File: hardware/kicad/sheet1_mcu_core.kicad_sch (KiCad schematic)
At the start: 0 parts

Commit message: feat: populate all 4 KiCad schematic sheets with embedded symbols and wiring
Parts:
- added U10: Raspberry_Pi_Pico, symbol HPVE:Pico
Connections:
- new net +3V3: U10.21 (GP16_MOSI)
- new net +5V: U10.39 (VSYS_5V)
- new net GND: U10.38 (GND)
- new net SPI_MOSI: U10.36 (3V3_OUT)
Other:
- title: Sheet 1: RP2040 Pico Core & I2C HUD -> Sheet 1: RP2040 Pico Core, Power & I2C UI
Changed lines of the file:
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@@
-(kicad_sch
-	(version 20230121)
-	(generator "HPVE_Hardware_Architect")
-	(generator_version "8.0")
-	(paper "A4")
+(kicad_sch (version 20230121) (generator "HPVE_Generator") (generator_version "8.0")
+	(paper "A3")
 	(title_block
-		(title "Sheet 1: RP2040 Pico Core & I2C HUD")
+		(title "Sheet 1: RP2040 Pico Core, Power & I2C UI")
 		(date "2026-10-30")
 		(rev "v1.0")
 		(company "Iron Cave Industries")
+		(comment 1 "Master System Brain & Telemetry Subsystem")
 	)
+	(symbol (lib_id "HPVE:Pico") (at 120.0 90.0 0) (unit 1)
+		(in_bom yes) (on_board yes) (dnp no)
+		(uuid "{gen_uuid()}")
+		(property "Reference" "U10" (at 120.0 60.0 0) (effects (font (size 1.27 1.27))))
+		(property "Value" "Raspberry_Pi_Pico" (at 120.0 120.0 0) (effects (font (size 1.27 1.27))))
+		(pin "6" (uuid "{gen_uuid()}"))
+		(pin "7" (uuid "{gen_uuid()}"))
+		(pin "14" (uuid "{gen_uuid()}"))
+		(pin "15" (uuid "{gen_uuid()}"))
+		(pin "16" (uuid "{gen_uuid()}"))
+		(pin "17" (uuid "{gen_uuid()}"))
+		(pin "21" (uuid "{gen_uuid()}"))
+		(pin "22" (uuid "{gen_uuid()}"))
+		(pin "24" (uuid "{gen_uuid()}"))
+		(pin "39" (uuid "{gen_uuid()}"))
+		(pin "36" (uuid "{gen_uuid()}"))
+		(pin "38" (uuid "{gen_uuid()}"))
+	)
+	(label "I2C_SDA" (at 102.22 110.32 180) (effects (font (size 1.016 1.016)) (justify right)) (uuid "{gen_uuid()}"))
+	(label "I2C_SCL" (at 102.22 105.24 180) (effects (font (size 1.016 1.016)) (justify right)) (uuid "{gen_uuid()}"))
+	(label "ENC_A1" (at 102.22 97.62 180) (effects (font (size 1.016 1.016)) (justify right)) (uuid "{gen_uuid()}"))
+	(label "ENC_B1" (at 102.22 92.54 180) (effects (font (size 1.016 1.016)) (justify right)) (uuid "{gen_uuid()}"))
+	(label "ENC_A2" (at 102.22 84.92 180) (effects (font (size 1.016 1.016)) (justify right)) (uuid "{gen_uuid()}"))
+	(label "ENC_B2" (at 102.22 79.84 180) (effects (font (size 1.016 1.016)) (justify right)) (uuid "{gen_uuid()}"))
+	(label "SPI_MOSI" (at 137.78 110.32 0) (effects (font (size 1.016 1.016)) (justify left)) (uuid "{gen_uuid()}"))
+	(label "SPI_SCK" (at 137.78 105.24 0) (effects (font (size 1.016 1.016)) (justify left)) (uuid "{gen_uuid()}"))
+	(label "SPI_LATCH" (at 137.78 100.16 0) (effects (font (size 1.016 1.016)) (justify left)) (uuid "{gen_uuid()}"))
+	(label "+5V" (at 120.0 62.06 90) (effects (font (size 1.016 1.016))) (uuid "{gen_uuid()}"))
+	(label "+3V3" (at 137.78 69.68 0) (effects (font (size 1.016 1.016)) (justify left)) (uuid "{gen_uuid()}"))
+	(label "GND" (at 120.0 117.94 270) (effects (font (size 1.016 1.016))) (uuid "{gen_uuid()}"))
 )

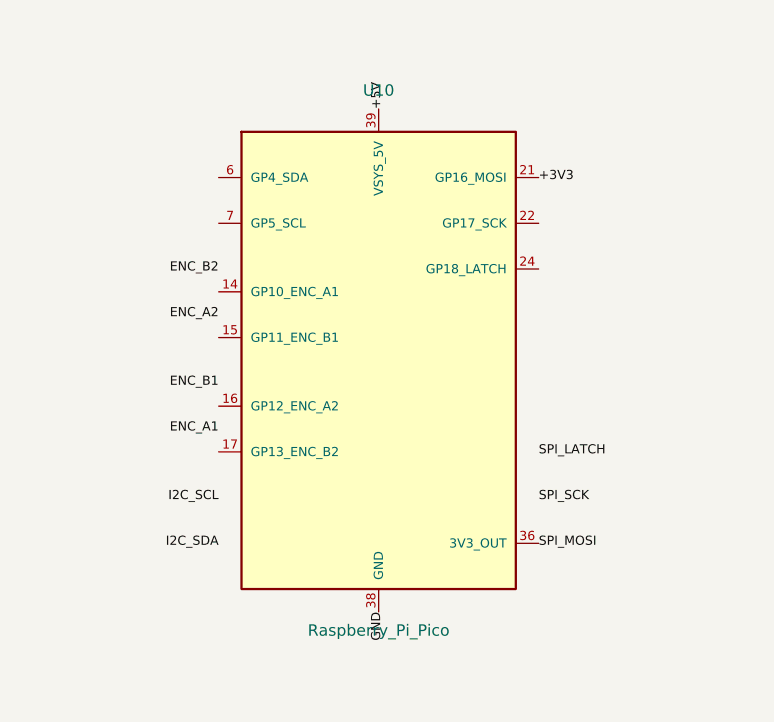
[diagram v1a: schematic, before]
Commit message: fix(kicad): assign valid footprints to all 105 symbols and add visible wiring
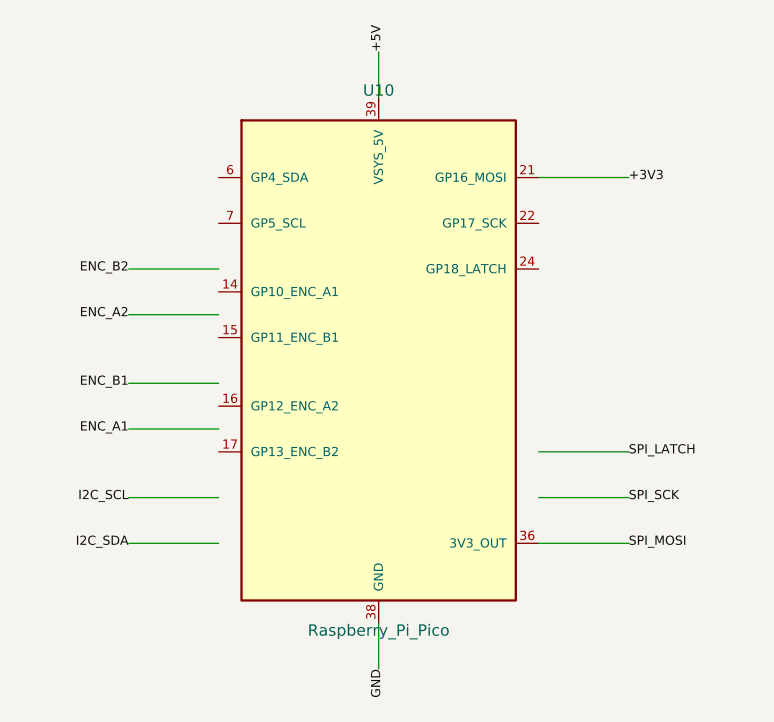
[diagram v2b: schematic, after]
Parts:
- U10: footprint (none) -> Connector_PinHeader_2.54mm:PinHeader_2x20_P2.54mm_Vertical
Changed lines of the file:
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@@
 		(property "Reference" "U10" (at 120.0 60.0 0) (effects (font (size 1.27 1.27))))
 		(property "Value" "Raspberry_Pi_Pico" (at 120.0 120.0 0) (effects (font (size 1.27 1.27))))
+		(property "Footprint" "Connector_PinHeader_2.54mm:PinHeader_2x20_P2.54mm_Vertical" (at 120.0 90.0 0) (effects (font (size 1.27 1.27)) hide))
 		(pin "6" (uuid "{gen_uuid()}"))
 		(pin "7" (uuid "{gen_uuid()}"))
@@
 		(pin "38" (uuid "{gen_uuid()}"))
 	)
-	(label "I2C_SDA" (at 102.22 110.32 180) (effects (font (size 1.016 1.016)) (justify right)) (uuid "{gen_uuid()}"))
-	(label "I2C_SCL" (at 102.22 105.24 180) (effects (font (size 1.016 1.016)) (justify right)) (uuid "{gen_uuid()}"))
-	(label "ENC_A1" (at 102.22 97.62 180) (effects (font (size 1.016 1.016)) (justify right)) (uuid "{gen_uuid()}"))
-	(label "ENC_B1" (at 102.22 92.54 180) (effects (font (size 1.016 1.016)) (justify right)) (uuid "{gen_uuid()}"))
-	(label "ENC_A2" (at 102.22 84.92 180) (effects (font (size 1.016 1.016)) (justify right)) (uuid "{gen_uuid()}"))
-	(label "ENC_B2" (at 102.22 79.84 180) (effects (font (size 1.016 1.016)) (justify right)) (uuid "{gen_uuid()}"))
-	(label "SPI_MOSI" (at 137.78 110.32 0) (effects (font (size 1.016 1.016)) (justify left)) (uuid "{gen_uuid()}"))
-	(label "SPI_SCK" (at 137.78 105.24 0) (effects (font (size 1.016 1.016)) (justify left)) (uuid "{gen_uuid()}"))
-	(label "SPI_LATCH" (at 137.78 100.16 0) (effects (font (size 1.016 1.016)) (justify left)) (uuid "{gen_uuid()}"))
-	(label "+5V" (at 120.0 62.06 90) (effects (font (size 1.016 1.016))) (uuid "{gen_uuid()}"))
-	(label "+3V3" (at 137.78 69.68 0) (effects (font (size 1.016 1.016)) (justify left)) (uuid "{gen_uuid()}"))
-	(label "GND" (at 120.0 117.94 270) (effects (font (size 1.016 1.016))) (uuid "{gen_uuid()}"))
+	(wire (pts (xy 102.22 110.32) (xy 92.22 110.32)) (stroke (width 0) (type default)) (uuid "{gen_uuid()}"))
+	(label "I2C_SDA" (at 92.22 110.32 180) (effects (font (size 1.016 1.016)) (justify right)) (uuid "{gen_uuid()}"))
+	(wire (pts (xy 102.22 105.24) (xy 92.22 105.24)) (stroke (width 0) (type default)) (uuid "{gen_uuid()}"))
+	(label "I2C_SCL" (at 92.22 105.24 180) (effects (font (size 1.016 1.016)) (justify right)) (uuid "{gen_uuid()}"))
+	(wire (pts (xy 102.22 97.62) (xy 92.22 97.62)) (stroke (width 0) (type default)) (uuid "{gen_uuid()}"))
+	(label "ENC_A1" (at 92.22 97.62 180) (effects (font (size 1.016 1.016)) (justify right)) (uuid "{gen_uuid()}"))
+	(wire (pts (xy 102.22 92.54) (xy 92.22 92.54)) (stroke (width 0) (type default)) (uuid "{gen_uuid()}"))
+	(label "ENC_B1" (at 92.22 92.54 180) (effects (font (size 1.016 1.016)) (justify right)) (uuid "{gen_uuid()}"))
+	(wire (pts (xy 102.22 84.92) (xy 92.22 84.92)) (stroke (width 0) (type default)) (uuid "{gen_uuid()}"))
+	(label "ENC_A2" (at 92.22 84.92 180) (effects (font (size 1.016 1.016)) (justify right)) (uuid "{gen_uuid()}"))
+	(wire (pts (xy 102.22 79.84) (xy 92.22 79.84)) (stroke (width 0) (type default)) (uuid "{gen_uuid()}"))
+	(label "ENC_B2" (at 92.22 79.84 180) (effects (font (size 1.016 1.016)) (justify right)) (uuid "{gen_uuid()}"))
+	(wire (pts (xy 137.78 110.32) (xy 147.78 110.32)) (stroke (width 0) (type default)) (uuid "{gen_uuid()}"))
+	(label "SPI_MOSI" (at 147.78 110.32 0) (effects (font (size 1.016 1.016)) (justify left)) (uuid "{gen_uuid()}"))
+	(wire (pts (xy 137.78 105.24) (xy 147.78 105.24)) (stroke (width 0) (type default)) (uuid "{gen_uuid()}"))
+	(label "SPI_SCK" (at 147.78 105.24 0) (effects (font (size 1.016 1.016)) (justify left)) (uuid "{gen_uuid()}"))
+	(wire (pts (xy 137.78 100.16) (xy 147.78 100.16)) (stroke (width 0) (type default)) (uuid "{gen_uuid()}"))
+	(label "SPI_LATCH" (at 147.78 100.16 0) (effects (font (size 1.016 1.016)) (justify left)) (uuid "{gen_uuid()}"))
+	(wire (pts (xy 120.0 60.79) (xy 120.0 55.71)) (stroke (width 0) (type default)) (uuid "{gen_uuid()}"))
+	(label "+5V" (at 120.0 55.71 90) (effects (font (size 1.016 1.016))) (uuid "{gen_uuid()}"))
+	(wire (pts (xy 137.78 69.68) (xy 147.78 69.68)) (stroke (width 0) (type default)) (uuid "{gen_uuid()}"))
+	(label "+3V3" (at 147.78 69.68 0) (effects (font (size 1.016 1.016)) (justify left)) (uuid "{gen_uuid()}"))
+	(wire (pts (xy 120.0 119.21) (xy 120.0 124.29)) (stroke (width 0) (type default)) (uuid "{gen_uuid()}"))
+	(label "GND" (at 120.0 124.29 270) (effects (font (size 1.016 1.016))) (uuid "{gen_uuid()}"))
 )

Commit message: Update KiCad symbols and netlist for spotless F8 PCB sync
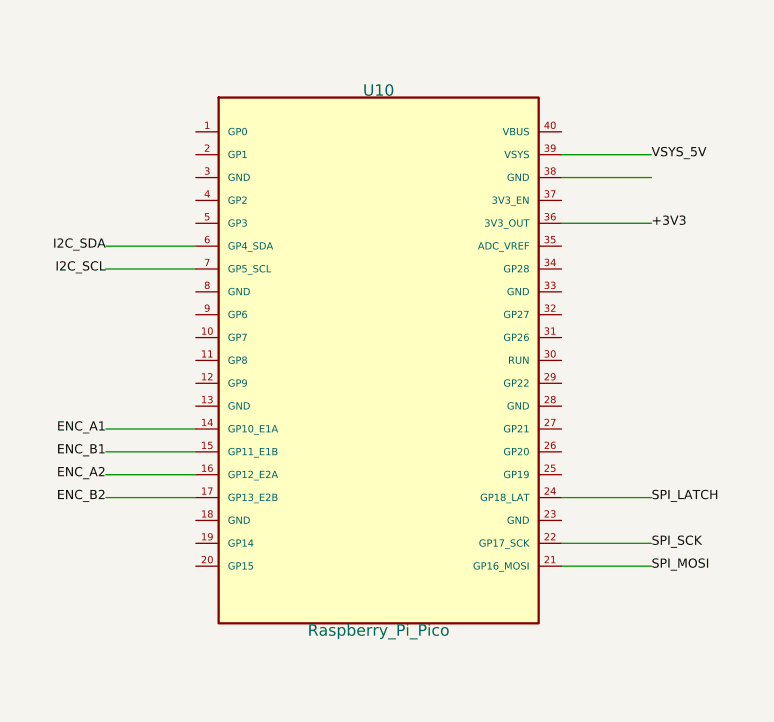
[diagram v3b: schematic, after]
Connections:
- net +3V3: now also U10.36 (3V3_OUT); no longer U10.21 (GP16_MOSI)
- net ENC_A1: now also U10.14 (GP10_E1A)
- net ENC_A2: now also U10.16 (GP12_E2A)
- net ENC_B1: now also U10.15 (GP11_E1B)
- net ENC_B2: now also U10.17 (GP13_E2B)
- net I2C_SCL: now also U10.7 (GP5_SCL)
- net I2C_SDA: now also U10.6 (GP4_SDA)
- net SPI_LATCH: now also U10.24 (GP18_LAT)
- net SPI_MOSI: now also U10.21 (GP16_MOSI); no longer U10.36 (3V3_OUT)
- net SPI_SCK: now also U10.22 (GP17_SCK)
- net +5V renamed VSYS_5V
- net GND: no longer names the net of U10.38 (GND)
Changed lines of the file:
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@@
 		(property "Value" "Raspberry_Pi_Pico" (at 120.0 120.0 0) (effects (font (size 1.27 1.27))))
 		(property "Footprint" "Connector_PinHeader_2.54mm:PinHeader_2x20_P2.54mm_Vertical" (at 120.0 90.0 0) (effects (font (size 1.27 1.27)) hide))
-		(pin "6" (uuid "{gen_uuid()}"))
-		(pin "7" (uuid "{gen_uuid()}"))
-		(pin "14" (uuid "{gen_uuid()}"))
-		(pin "15" (uuid "{gen_uuid()}"))
-		(pin "16" (uuid "{gen_uuid()}"))
-		(pin "17" (uuid "{gen_uuid()}"))
-		(pin "21" (uuid "{gen_uuid()}"))
-		(pin "22" (uuid "{gen_uuid()}"))
-		(pin "24" (uuid "{gen_uuid()}"))
-		(pin "39" (uuid "{gen_uuid()}"))
-		(pin "36" (uuid "{gen_uuid()}"))
-		(pin "38" (uuid "{gen_uuid()}"))
+		(pin "1")
+		(pin "2")
+		(pin "3")
+		(pin "4")
+		(pin "5")
+		(pin "6")
+		(pin "7")
+		(pin "8")
+		(pin "9")
+		(pin "10")
+		(pin "11")
+		(pin "12")
+		(pin "13")
+		(pin "14")
+		(pin "15")
+		(pin "16")
+		(pin "17")
+		(pin "18")
+		(pin "19")
+		(pin "20")
+		(pin "21")
+		(pin "22")
+		(pin "23")
+		(pin "24")
+		(pin "25")
+		(pin "26")
+		(pin "27")
+		(pin "28")
+		(pin "29")
+		(pin "30")
+		(pin "31")
+		(pin "32")
+		(pin "33")
+		(pin "34")
+		(pin "35")
+		(pin "36")
+		(pin "37")
+		(pin "38")
+		(pin "39")
+		(pin "40")
 	)
-	(wire (pts (xy 102.22 110.32) (xy 92.22 110.32)) (stroke (width 0) (type default)) (uuid "{gen_uuid()}"))
-	(label "I2C_SDA" (at 92.22 110.32 180) (effects (font (size 1.016 1.016)) (justify right)) (uuid "{gen_uuid()}"))
-	(wire (pts (xy 102.22 105.24) (xy 92.22 105.24)) (stroke (width 0) (type default)) (uuid "{gen_uuid()}"))
-	(label "I2C_SCL" (at 92.22 105.24 180) (effects (font (size 1.016 1.016)) (justify right)) (uuid "{gen_uuid()}"))
-	(wire (pts (xy 102.22 97.62) (xy 92.22 97.62)) (stroke (width 0) (type default)) (uuid "{gen_uuid()}"))
-	(label "ENC_A1" (at 92.22 97.62 180) (effects (font (size 1.016 1.016)) (justify right)) (uuid "{gen_uuid()}"))
-	(wire (pts (xy 102.22 92.54) (xy 92.22 92.54)) (stroke (width 0) (type default)) (uuid "{gen_uuid()}"))
-	(label "ENC_B1" (at 92.22 92.54 180) (effects (font (size 1.016 1.016)) (justify right)) (uuid "{gen_uuid()}"))
-	(wire (pts (xy 102.22 84.92) (xy 92.22 84.92)) (stroke (width 0) (type default)) (uuid "{gen_uuid()}"))
-	(label "ENC_A2" (at 92.22 84.92 180) (effects (font (size 1.016 1.016)) (justify right)) (uuid "{gen_uuid()}"))
-	(wire (pts (xy 102.22 79.84) (xy 92.22 79.84)) (stroke (width 0) (type default)) (uuid "{gen_uuid()}"))
-	(label "ENC_B2" (at 92.22 79.84 180) (effects (font (size 1.016 1.016)) (justify right)) (uuid "{gen_uuid()}"))
-	(wire (pts (xy 137.78 110.32) (xy 147.78 110.32)) (stroke (width 0) (type default)) (uuid "{gen_uuid()}"))
-	(label "SPI_MOSI" (at 147.78 110.32 0) (effects (font (size 1.016 1.016)) (justify left)) (uuid "{gen_uuid()}"))
-	(wire (pts (xy 137.78 105.24) (xy 147.78 105.24)) (stroke (width 0) (type default)) (uuid "{gen_uuid()}"))
-	(label "SPI_SCK" (at 147.78 105.24 0) (effects (font (size 1.016 1.016)) (justify left)) (uuid "{gen_uuid()}"))
-	(wire (pts (xy 137.78 100.16) (xy 147.78 100.16)) (stroke (width 0) (type default)) (uuid "{gen_uuid()}"))
-	(label "SPI_LATCH" (at 147.78 100.16 0) (effects (font (size 1.016 1.016)) (justify left)) (uuid "{gen_uuid()}"))
-	(wire (pts (xy 120.0 60.79) (xy 120.0 55.71)) (stroke (width 0) (type default)) (uuid "{gen_uuid()}"))
-	(label "+5V" (at 120.0 55.71 90) (effects (font (size 1.016 1.016))) (uuid "{gen_uuid()}"))
-	(wire (pts (xy 137.78 69.68) (xy 147.78 69.68)) (stroke (width 0) (type default)) (uuid "{gen_uuid()}"))
-	(label "+3V3" (at 147.78 69.68 0) (effects (font (size 1.016 1.016)) (justify left)) (uuid "{gen_uuid()}"))
-	(wire (pts (xy 120.0 119.21) (xy 120.0 124.29)) (stroke (width 0) (type default)) (uuid "{gen_uuid()}"))
-	(label "GND" (at 120.0 124.29 270) (effects (font (size 1.016 1.016))) (uuid "{gen_uuid()}"))
+	(wire (pts (xy 99.68 77.30) (xy 89.68 77.30)) (stroke (width 0) (type default)) (uuid "{gen_uuid()}"))
+	(label "I2C_SDA" (at 89.68 77.30 180) (effects (font (size 1.016 1.016)) (justify right)) (uuid "{gen_uuid()}"))
+	(wire (pts (xy 99.68 79.84) (xy 89.68 79.84)) (stroke (width 0) (type default)) (uuid "{gen_uuid()}"))
+	(label "I2C_SCL" (at 89.68 79.84 180) (effects (font (size 1.016 1.016)) (justify right)) (uuid "{gen_uuid()}"))
+	(wire (pts (xy 99.68 97.62) (xy 89.68 97.62)) (stroke (width 0) (type default)) (uuid "{gen_uuid()}"))
+	(label "ENC_A1" (at 89.68 97.62 180) (effects (font (size 1.016 1.016)) (justify right)) (uuid "{gen_uuid()}"))
+	(wire (pts (xy 99.68 100.16) (xy 89.68 100.16)) (stroke (width 0) (type default)) (uuid "{gen_uuid()}"))
+	(label "ENC_B1" (at 89.68 100.16 180) (effects (font (size 1.016 1.016)) (justify right)) (uuid "{gen_uuid()}"))
+	(wire (pts (xy 99.68 102.70) (xy 89.68 102.70)) (stroke (width 0) (type default)) (uuid "{gen_uuid()}"))
+	(label "ENC_A2" (at 89.68 102.70 180) (effects (font (size 1.016 1.016)) (justify right)) (uuid "{gen_uuid()}"))
+	(wire (pts (xy 99.68 105.24) (xy 89.68 105.24)) (stroke (width 0) (type default)) (uuid "{gen_uuid()}"))
+	(label "ENC_B2" (at 89.68 105.24 180) (effects (font (size 1.016 1.016)) (justify right)) (uuid "{gen_uuid()}"))
+	(wire (pts (xy 140.32 112.86) (xy 150.32 112.86)) (stroke (width 0) (type default)) (uuid "{gen_uuid()}"))
+	(label "SPI_MOSI" (at 150.32 112.86 0) (effects (font (size 1.016 1.016)) (justify left)) (uuid "{gen_uuid()}"))
+	(wire (pts (xy 140.32 110.32) (xy 150.32 110.32)) (stroke (width 0) (type default)) (uuid "{gen_uuid()}"))
+	(label "SPI_SCK" (at 150.32 110.32 0) (effects (font (size 1.016 1.016)) (justify left)) (uuid "{gen_uuid()}"))
+	(wire (pts (xy 140.32 105.24) (xy 150.32 105.24)) (stroke (width 0) (type default)) (uuid "{gen_uuid()}"))
+	(label "SPI_LATCH" (at 150.32 105.24 0) (effects (font (size 1.016 1.016)) (justify left)) (uuid "{gen_uuid()}"))
+	(wire (pts (xy 140.32 67.14) (xy 150.32 67.14)) (stroke (width 0) (type default)) (uuid "{gen_uuid()}"))
+	(label "VSYS_5V" (at 150.32 67.14 0) (effects (font (size 1.016 1.016)) (justify left)) (uuid "{gen_uuid()}"))
+	(wire (pts (xy 140.32 74.76) (xy 150.32 74.76)) (stroke (width 0) (type default)) (uuid "{gen_uuid()}"))
+	(label "+3V3" (at 150.32 74.76 0) (effects (font (size 1.016 1.016)) (justify left)) (uuid "{gen_uuid()}"))
+	(wire (pts (xy 140.32 69.68) (xy 150.32 69.68)) (stroke (width 0) (type default)) (uuid "{gen_uuid()}"))
 )
